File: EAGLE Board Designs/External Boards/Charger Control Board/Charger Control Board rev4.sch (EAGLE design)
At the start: 83 parts, among them U1 CPC1002N

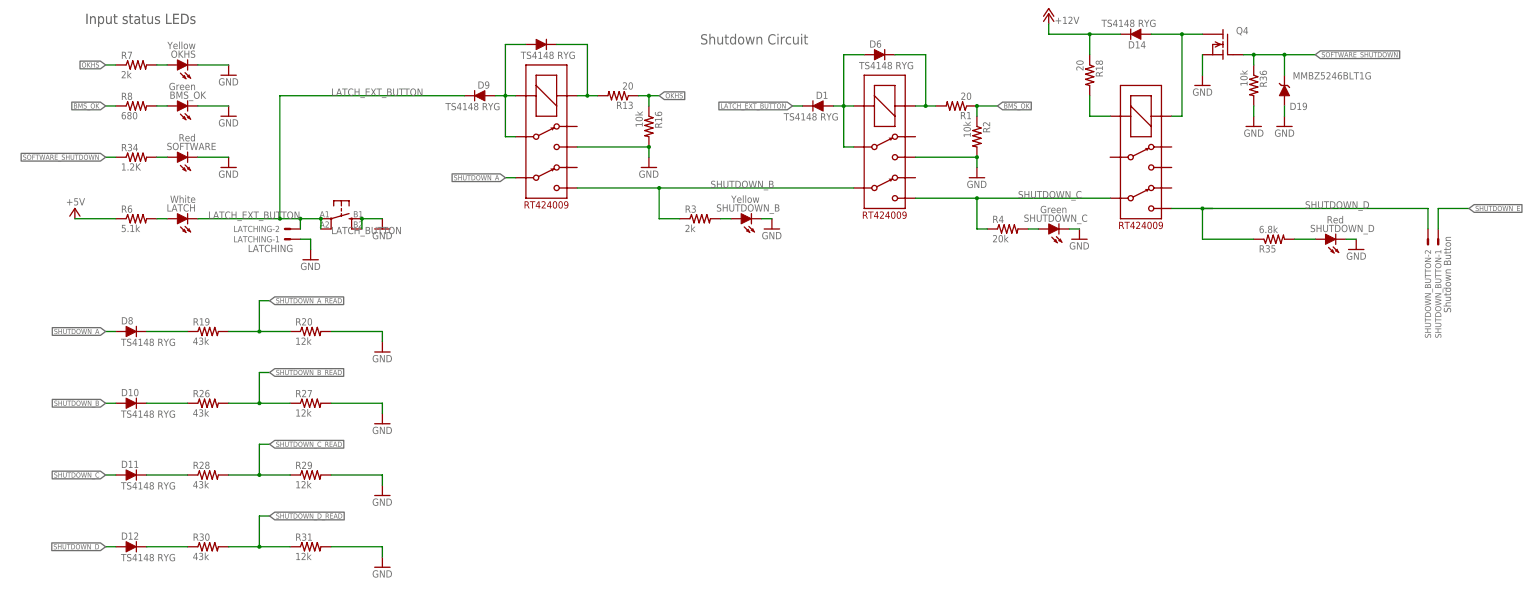
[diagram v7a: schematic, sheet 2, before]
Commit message: Finalized and renumbered board
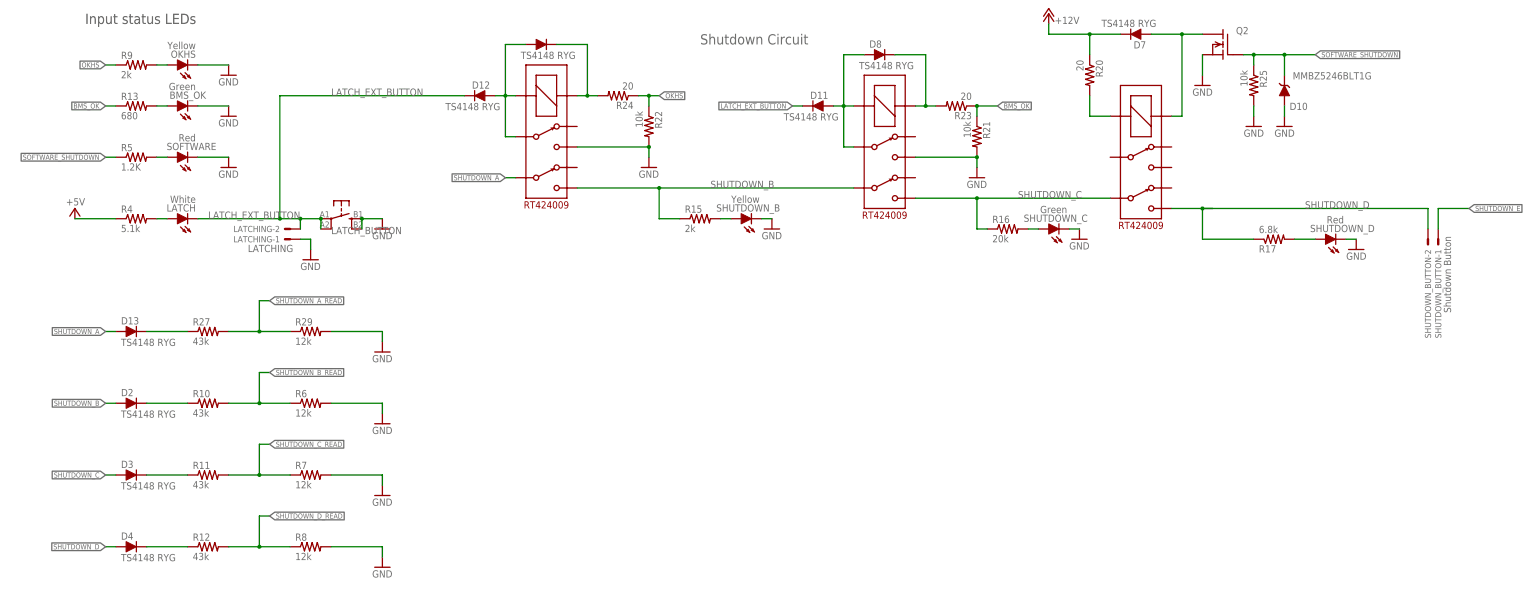
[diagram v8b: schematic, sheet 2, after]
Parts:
- removed D14: TS4148 RYG, HyTechDevices:DIODE0805
- removed D19: MMBZ5246BLT1G, HyTechDevices:DIODE_ZENER
- removed R30: 43k, HyTechDevices:RESISTOR0603-RES
- removed R31: 12k, HyTechDevices:RESISTOR0603-RES
- removed R34: 1.2K, HyTechDevices:RESISTOR0603-RES
- removed R35: 6.8k, HyTechDevices:RESISTOR0603-RES
- removed ZENER: DIODE_ZENER, HyTechDevices:DIODE_ZENER
- added D13, D4: TS4148 RYG, HyTechDevices:DIODE0805
- added D5: DIODE_ZENER0603, HyTechDevices:DIODE_ZENER0603
- added R21, R22: 10k, HyTechDevices:RESISTOR0603-RES
- added R23, R24: 20, HyTechDevices:RESISTOR0603-RES
- C1: value 1uF -> 10uF; TOLERANCE 5% -> 1%; VOLTAGE 10V -> 25V
- C2: value .1uF -> 10uF; VOLTAGE 10V -> 25V
- C3: value 10uF -> 4.7nF; TOLERANCE 1% -> 5%; VOLTAGE 25V -> 50V
- C4: value 10uF -> 1uF; VOLTAGE 25V -> 10V
- C5: value 4.7nF -> .1uF; VOLTAGE 50V -> 10V
- D1: value TS4148 RYG -> DIODE
- D10: value TS4148 RYG -> MMBZ5246BLT1G; device HyTechDevices:DIODE0805 -> HyTechDevices:DIODE_ZENER
- D2: value DIODE_ZENER0603 -> TS4148 RYG; device HyTechDevices:DIODE_ZENER0603 -> HyTechDevices:DIODE0805
- D3: value DIODE -> TS4148 RYG
- D6: value TS4148 RYG -> DIODE_ZENER; device HyTechDevices:DIODE0805 -> HyTechDevices:DIODE_ZENER
- R1: value 20 -> 68
- R10: value 60 -> 43k; TOLERANCE 1% -> (none)
- R11: value 20k -> 43k; TOLERANCE 1% -> (none)
- R12: value 5.1k -> 43k; TOLERANCE 1% -> (none)
- R13: value 20 -> 680
- R14: value 360 -> 270
- R15: value 68 -> 2k
- R16: value 10k -> 20k
- R17: value 68 -> 6.8k; TOLERANCE 1% -> (none)
- R18: value 20 -> 5.1k
- R19: value 43k -> 20k; TOLERANCE (none) -> 1%
- R2: value 10k -> 360
- R20: value 12k -> 20; TOLERANCE (none) -> 1%
- R26, R28: value 43k -> 60; TOLERANCE (none) -> 1%
- R27: value 12k -> 43k
- R3: value 2k -> 68
- R4: value 20k -> 5.1k
- R5: value 270 -> 1.2K; TOLERANCE 1% -> (none)
- R6: value 5.1k -> 12k; TOLERANCE 1% -> (none)
- R7: value 2k -> 12k; TOLERANCE 1% -> (none)
- R8: value 680 -> 12k; TOLERANCE 1% -> (none)
- R9: value 60 -> 2k
- U$3: value KT12-1A-40L-THT -> TEENSY_3.5_EXT_RTC; device HyTechDevices:KT12-1A-40L-THT -> HyTechDevices:TEENSY_3.5_EXT_RTC
- U$5: value TEENSY_3.5_EXT_RTC -> KT12-1A-40L-THT; device HyTechDevices:TEENSY_3.5_EXT_RTC -> HyTechDevices:KT12-1A-40L-THT
- renumbered Q4 to Q2, R36 to R25, STATUS_3.5 to STATUS_3.1, U$1 to U2, U$16 to $$U$3
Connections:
- net +12V: now also C1.2, D7.C, R20.1; no longer C3.2, D14.C, R18.1
- net +12VIN: now also D5.C; no longer D2.C
- net +5V: now also C5.2, R14.1, R4.1, U$3.VIN; no longer C1.2, R5.1, R6.1, U$5.VIN
- net BMS_OK: now also R13.1, R21.1, R23.1; no longer R1.1, R2.1, R8.1
- net BMS_OK_RELAY: now also D8.C, R23.2; no longer D6.C, R1.2
- net BMS_PWR_STEP: now also D11.A, D8.A; no longer D1.A, D6.A
- net CANL: now also R28.1; no longer R9.1
- net CHARGER_1: now also U$5.S1; no longer U$3.S1
- net CHARGER_2: now also U$5.S2; no longer U$3.S2
- net CHARGE_CONTROL: now also D1.C, U$5.C2; no longer D3.C, U$3.C2
- net CHARGE_ENABLE: now also D6.C, R19.2; no longer R11.2, ZENER.C
- net GND: now also C3.2, C5.1, D1.A, D10.A, D5.A, D6.A, R18.1, R21.2, R22.2, R6.2, R7.2, R8.2, U$3.GND, U$5.C1; no longer C3.1, C5.2, D19.A, D2.A, D3.A, R12.1, R16.2, R2.2, R20.2, R27.2, R31.2, U$3.C1, U$5.GND, ZENER.A
- net IMD_PWR_STEP: now also D12.A; no longer D7.A
- net LATCH_EXT_BUTTON: now also D11.C, D12.C; no longer D1.C, D9.C
- net N$10: now also R2.2; no longer R14.2
- net N$11: now also R3.2; no longer R15.2
- net N$12: now also D9.C, R24.2; no longer D7.C, R13.2
- net N$13: now also R20.2; no longer R18.2
- net N$14: now also D13.C, R27.1; no longer D8.C, R19.1
- net N$17: now also R26.2; no longer R10.2
- net N$18: now also D2.C, R10.1; no longer D10.C, R26.1
- net N$19: now also R15.2; no longer R3.2
- net N$2: now also R4.2; no longer R6.2
- net N$20: now also D3.C, R11.1; no longer D11.C, R28.1
- net N$21: now also D4.C, R12.1; no longer D12.C, R30.1
- net N$26: now also R9.2; no longer R7.2
- net N$29: now also R14.2; no longer R5.2
- net N$3: now also R13.2; no longer R8.2
- net N$30: now also R17.2; no longer R35.2
- net N$31: now also R5.2; no longer R34.2
- net N$32: now also R16.2; no longer R4.2
- net N$33: now also D7.A; no longer D14.A
- net N$4: now also U$3.D4(CANRX); no longer U$5.D4(CANRX)
- net N$5: now also R18.2, R19.1; no longer R11.1, R12.2
- net N$6: now also U$3.D3(CANTX); no longer U$5.D3(CANTX)
- net N$61: now also U$3.GND2; no longer U$5.GND2
- net N$62: now also C3.1, R26.1, R28.2; no longer C5.1, R10.1, R9.2
- net N$7: now also R1.1; no longer R17.1
- net N$8: now also R3.1; no longer R15.1
- net N$9: now also R1.2, U$3.D8(TX3); no longer R17.2, U$5.D8(TX3)
- net OKHS: now also R22.1, R24.1, R9.1; no longer R13.1, R16.1, R7.1
- net SHUTDOWN_A: now also D13.A; no longer D8.A
- net SHUTDOWN_A_READ: now also R27.2, R29.1; no longer R19.2, R20.1
- net SHUTDOWN_B: now also D2.A, R15.1; no longer D10.A, R3.1
- net SHUTDOWN_B_READ: now also R10.2, R6.1; no longer R26.2, R27.1
- net SHUTDOWN_C: now also D3.A, R16.1; no longer D11.A, R4.1
- net SHUTDOWN_C_READ: now also R11.2, R7.1; no longer R28.2, R29.1
- net SHUTDOWN_D: now also D4.A, R17.1; no longer D12.A, R35.1
- net SHUTDOWN_D_READ: now also R12.2, R8.1; no longer R30.2, R31.1
- net SOFTWARE_SHUTDOWN: now also D10.C, R5.1; no longer D19.C, R34.1
- net TOGGLE_CHARGER: now also R2.1; no longer R14.1
- net VBAT_RTC: now also U$3.VBAT; no longer U$5.VBAT
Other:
- moved on the sheet: C1, C2, C3, C4, C5, D11, D12, D8, R13, R14, R16, R20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
